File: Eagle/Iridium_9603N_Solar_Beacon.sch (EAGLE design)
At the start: 55 parts, among them CON2 uFL, J1 SS4-10-3.50-X-D, Q1 DMG3415U-7, Q2 2N2222, Q3 DMG3415U-7, U1 MCP111T-240E/TT, U2 SPX3819-3.3, U3 LTC3225EDDB#TRMPBF, U4 AS179-92LF, U5 ATSAMD21G18_QFN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

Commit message: Updated the PCB
Updated the PCB to improve the ground paths around the SAMD; added extra decoupling capacitors. Minor updates to the Arduino code.
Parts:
- added C14, C15: 10µF, microbuilder:CAP_CERAMIC0805-NOOUTLINE
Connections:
- net +3V3: now also C14.1, C15.1
- net GND: now also C14.2, C15.2
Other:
- moved on the sheet: C1, C11

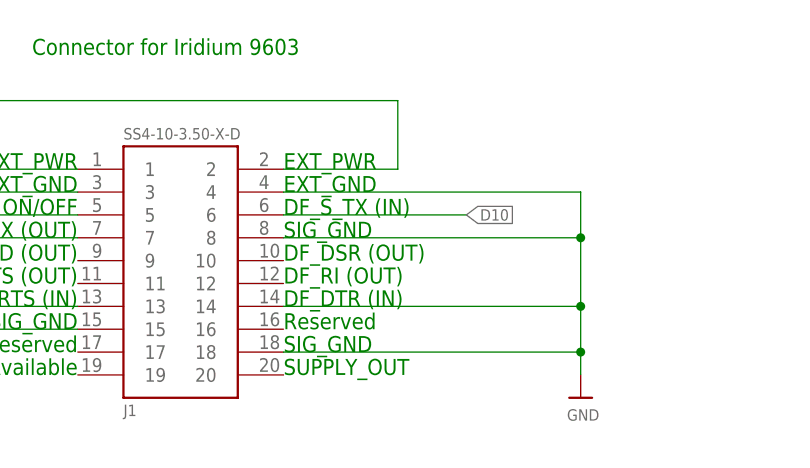
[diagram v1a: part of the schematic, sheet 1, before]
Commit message: Connected the Ring Indicator
Connected the 9603N Ring Indicator to D21 just in case the solar beacon is used as a very compact Beacon Base (powered by USB).
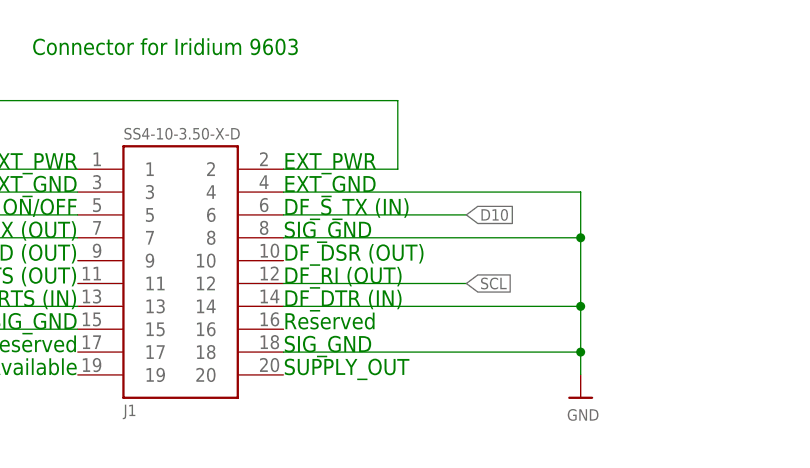
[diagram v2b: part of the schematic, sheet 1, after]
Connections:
- net SCL: now also J1.12
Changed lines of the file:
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@@
+</segment>
+</net>
+<net name="SCL" class="0">
+<segment>
+<pinref part="J1" gate="G$1" pin="12"/>
+<wire x1="96.52" y1="38.1" x2="116.84" y2="38.1" width="0.1524" layer="91"/>
+<label x="116.84" y="38.1" size="1.27" layer="95" xref="yes"/>
 </segment>
 </net>

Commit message: Corrected the zero width polygons
Corrected the zero width polygons in the micro USB connector that would have caused problems for OSH Park. Thanks go to Paul Loewen @ usask.ca
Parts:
- CON1: device microbuilder:USBFCI_10103594 -> Iridium_9603_Beacon:MICROBUILDER_USBFCI_10103594_CORRECTED
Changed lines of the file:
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@@
 <layer number="59" name="tCarbon" color="7" fill="1" visible="no" active="no"/>
 <layer number="60" name="bCarbon" color="7" fill="1" visible="no" active="no"/>
+<layer number="88" name="SimResults" color="9" fill="1" visible="yes" active="yes"/>
+<layer number="89" name="SimProbes" color="9" fill="1" visible="yes" active="yes"/>
 <layer number="90" name="Modules" color="5" fill="1" visible="yes" active="yes"/>
 <layer number="91" name="Nets" color="2" fill="1" visible="yes" active="yes"/>
@@
 <part name="U$31" library="microbuilder" deviceset="GND" device=""/>
 <part name="SW1" library="SparkFun-Electromechanical" deviceset="SWITCH_SPST_4_PIN" device="RECT"/>
-<part name="CON1" library="microbuilder" deviceset="USB" device="FCI_10103594"/>
+<part name="CON1" library="Iridium_9603_Beacon" deviceset="MICROBUILDER_USB" device="FCI_10103594_CORRECTED"/>
 <part name="FD1" library="SparkFun-Aesthetics" deviceset="FIDUCIAL" device="1X2"/>
 <part name="FD2" library="SparkFun-Aesthetics" deviceset="FIDUCIAL" device="1X2"/>
